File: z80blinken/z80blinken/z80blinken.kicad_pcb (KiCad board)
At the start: 4 copper layers, 101.6 x 53.3 mm, 22 parts, among them J1 RCBus-80, J2 ADDR, J3 CTRL, J4 DATA, J5 A16_A23, J7 USER, SW1 RESET, U1 Z80CPU

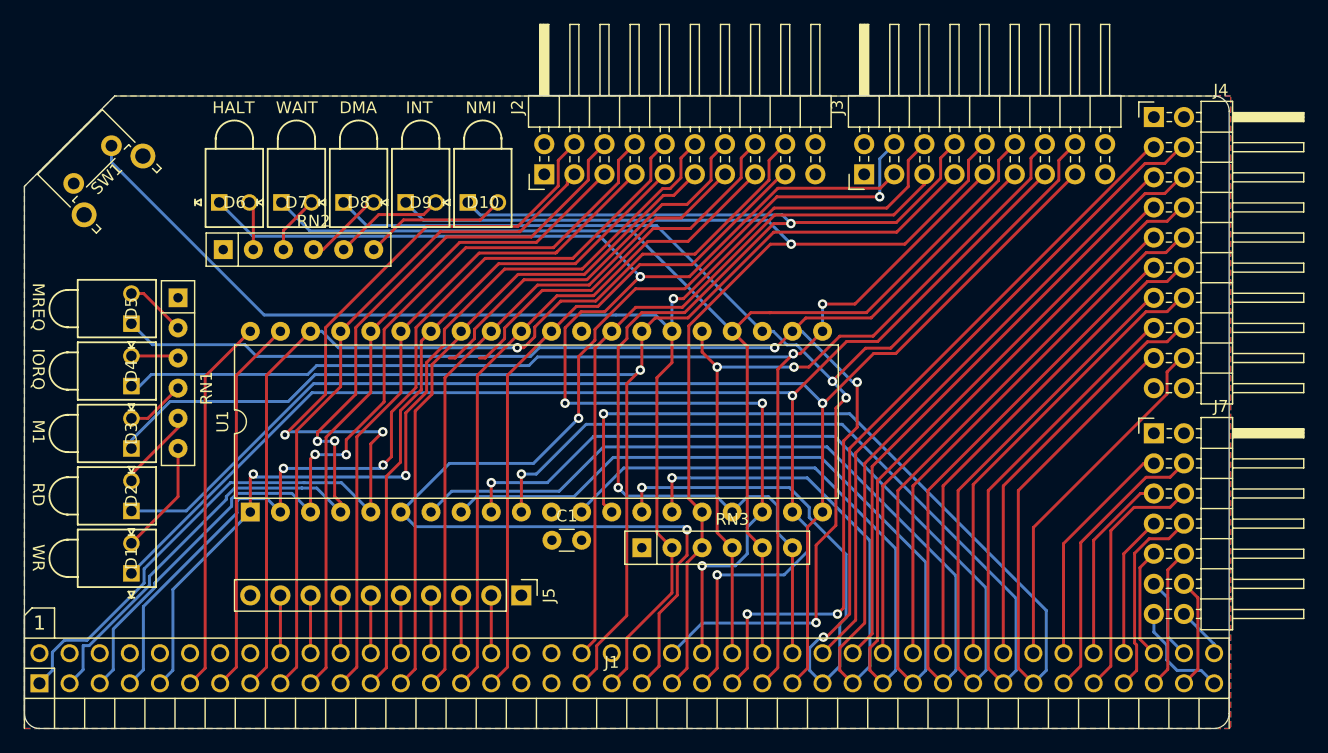
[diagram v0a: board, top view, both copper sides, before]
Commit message: Remove test points; finish silkscreen
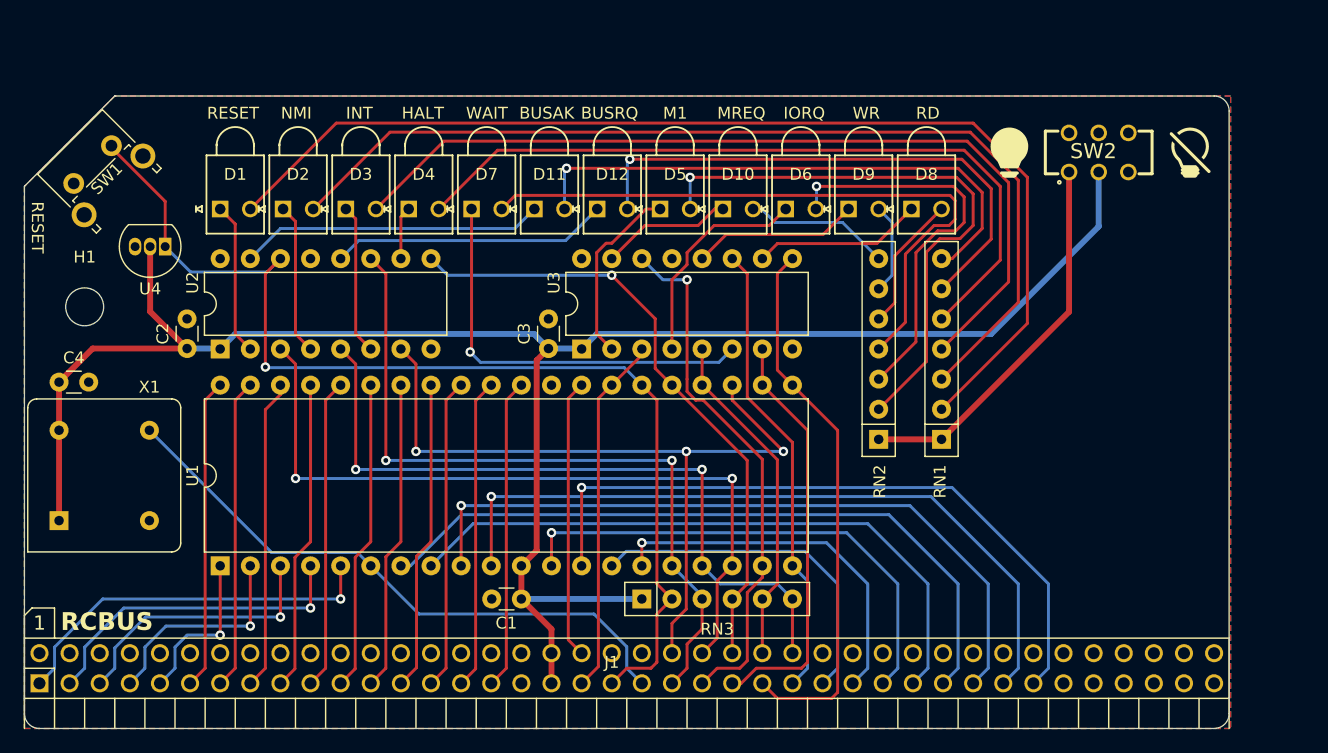
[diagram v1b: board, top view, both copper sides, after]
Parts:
- removed J2: ADDR, Connector_PinHeader_2.54mm:PinHeader_2x10_P2.54mm_Horizontal
- removed J3: CTRL, Connector_PinHeader_2.54mm:PinHeader_2x09_P2.54mm_Horizontal
- removed J4: DATA, Connector_PinHeader_2.54mm:PinHeader_2x10_P2.54mm_Horizontal
- removed J5: A16_A23, Connector_PinHeader_2.54mm:PinHeader_1x10_P2.54mm_Vertical
- removed J7: USER, Connector_PinHeader_2.54mm:PinHeader_2x07_P2.54mm_Horizontal
- added C2: 0.1uf, Capacitor_THT:C_Disc_D3.0mm_W1.6mm_P2.50mm, F.Cu at (102.6, 95.0)
- added C3: 0.1uf, Capacitor_THT:C_Disc_D3.0mm_W1.6mm_P2.50mm, F.Cu at (133.1, 95.0)
- added C4: 0.1uf, Capacitor_THT:C_Disc_D3.0mm_W1.6mm_P2.50mm, F.Cu at (91.8, 97.8)
- added D11: LED, Custom:LED_WP934CB&slash_GD_KNB, F.Cu at (131.9, 83.2)
- added D12: LED, Custom:LED_WP934CB&slash_GD_KNB, F.Cu at (137.2, 83.2)
- added H1: MountingHole, MountingHole:MountingHole_3.2mm_M3, F.Cu at (94.0, 91.4)
- added SW2: SW_SPST, SamacSys_Parts:JS202011CQN, F.Cu at (179.5, 78.4)
- added U2: 4050, Package_DIP:DIP-16_W7.62mm, F.Cu at (105.4, 95.0)
- added U3: 4050, Package_DIP:DIP-16_W7.62mm, F.Cu at (135.9, 95.0)
- added U4: MCP100-475D, Package_TO_SOT_THT:TO-92_Inline, F.Cu at (100.8, 86.4)
- added X1: CXO_DIP8, Oscillator:Oscillator_DIP-8, F.Cu at (91.8, 109.5)
- RN1, RN2: footprint Resistor_THT:R_Array_SIP6 -> Resistor_THT:R_Array_SIP7
- moved RN1 65.5 mm to (166.2, 102.6), turned to 90 degrees
- moved RN2 57.5 mm to (160.9, 102.6), turned to 90 degrees
- moved D8 47.9 mm to (163.7, 83.2)
- moved D6 47.8 mm to (153.1, 83.2)
- moved D5 45.6 mm to (142.5, 83.2), turned to 0 degrees
- moved D9 37.4 mm to (158.4, 83.2)
- moved D1 31.6 mm to (105.4, 83.2), turned to 0 degrees
- moved D2 28.5 mm to (110.7, 83.2), turned to 0 degrees
- moved D4 27.7 mm to (121.3, 83.2), turned to 0 degrees
- moved D3 27.1 mm to (116.0, 83.2), turned to 0 degrees
- moved D10 21.5 mm to (147.8, 83.2)
- moved D7 16.0 mm to (126.6, 83.2)
- moved C1 5.58 mm to (130.8, 116.1), turned to 180 degrees
- moved U1 5.20 mm to (105.4, 113.3)
- moved RN3 4.32 mm to (141.0, 116.1)
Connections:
- D1 pad 1: /~{MREQ} -> Net-(D1-K)
- D10 pad 1: /~{NMI} -> Net-(D10-K)
- D2 pad 1: /~{IORQ} -> Net-(D2-K)
- D3 pad 1: /~{M1} -> Net-(D3-K)
- D4 pad 1: /~{RD} -> Net-(D4-K)
- D5 pad 1: /~{WR} -> Net-(D5-K)
- D6 pad 1: /~{HALT} -> Net-(D6-K)
- D7 pad 1: /~{WAIT} -> Net-(D7-K)
- D8 pad 1: /~{BUSACK} -> Net-(D8-K)
- D9 pad 1: /~{INT} -> Net-(D9-K)
- RN1 pad 1: +5V -> Net-(RN1-common)
- RN1 pad 2: Net-(D5-A) -> Net-(D1-A)
- RN1 pad 3: Net-(D4-A) -> Net-(D2-A)
- RN1 pad 5: Net-(D2-A) -> Net-(D4-A)
- RN1 pad 6: Net-(D1-A) -> Net-(D12-A)
- RN2 pad 1: +5V -> Net-(RN1-common)
- RN2 pad 2: Net-(D6-A) -> Net-(D5-A)
- RN2 pad 3: Net-(D7-A) -> Net-(D6-A)
- RN2 pad 4: Net-(D8-A) -> Net-(D7-A)
- RN2 pad 5: Net-(D9-A) -> Net-(D8-A)
- RN2 pad 6: Net-(D10-A) -> Net-(D9-A)
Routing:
- net +5V: track 0.00 -> 160.9 mm
- net /~{WR}: track 123.5 -> 35.1 mm, vias 4 -> 0
- net Net-(D1-A): track 9.63 -> 93.0 mm
- net /~{M1}: track 109.7 -> 30.3 mm, vias 1 -> 0
- net /~{IORQ}: track 117.4 -> 39.0 mm, vias 1 -> 0
- net /~{MREQ}: track 123.0 -> 44.8 mm, vias 2 -> 1
- net Net-(D2-A): track 6.90 -> 83.3 mm
- net /~{WAIT}: track 102.1 -> 28.8 mm
- net Net-(D3-A): track 4.99 -> 73.5 mm
- net /~{RD}: track 109.6 -> 46.3 mm, vias 2 -> 0
- net /A11: track 76.2 -> 13.6 mm, vias 2 -> 1
- net /D0: track 91.7 -> 29.6 mm, vias 2 -> 0
- net /A15: track 92.2 -> 32.2 mm, vias 2 -> 1
- net Net-(D4-A): track 4.00 -> 63.9 mm
- net /A12: track 76.9 -> 18.3 mm, vias 2 -> 1
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- added copper zone on F.Cu, net GND
- removed copper zone on F.Cu, net +5V
- removed copper zone on In2.Cu, net +5V
- removed copper zone on In1.Cu, net GND
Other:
- copper layers 4 -> 2
- board text added: "BUSAK"
- board text added: "BUSRQ"
- board text added: "HEX BUFFER CD4050BE"
- board text added: "RCBUS"
- board text added: "RESET"
- board text added: "Z80"
- board text added: "Z80blinken © 2024 J.B. Langston https://github.com/jblang/z80ctrl"
- board text removed: "DMA"
